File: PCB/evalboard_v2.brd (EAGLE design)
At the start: 85.7 x 65.5 mm, 63 parts, among them IC1 BQ24074, IC2 LTC3113EFE#PBF, IC3 LTC3130IUDC-1#PBF#2, J1 2604-1102, J2 PJ-031D, J3 2604-1102, Q1 DMP3056L-7#2, Q2 DMG3402L-7, Q3 DMP3056L-7#2, Q4 DMG3402L-7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

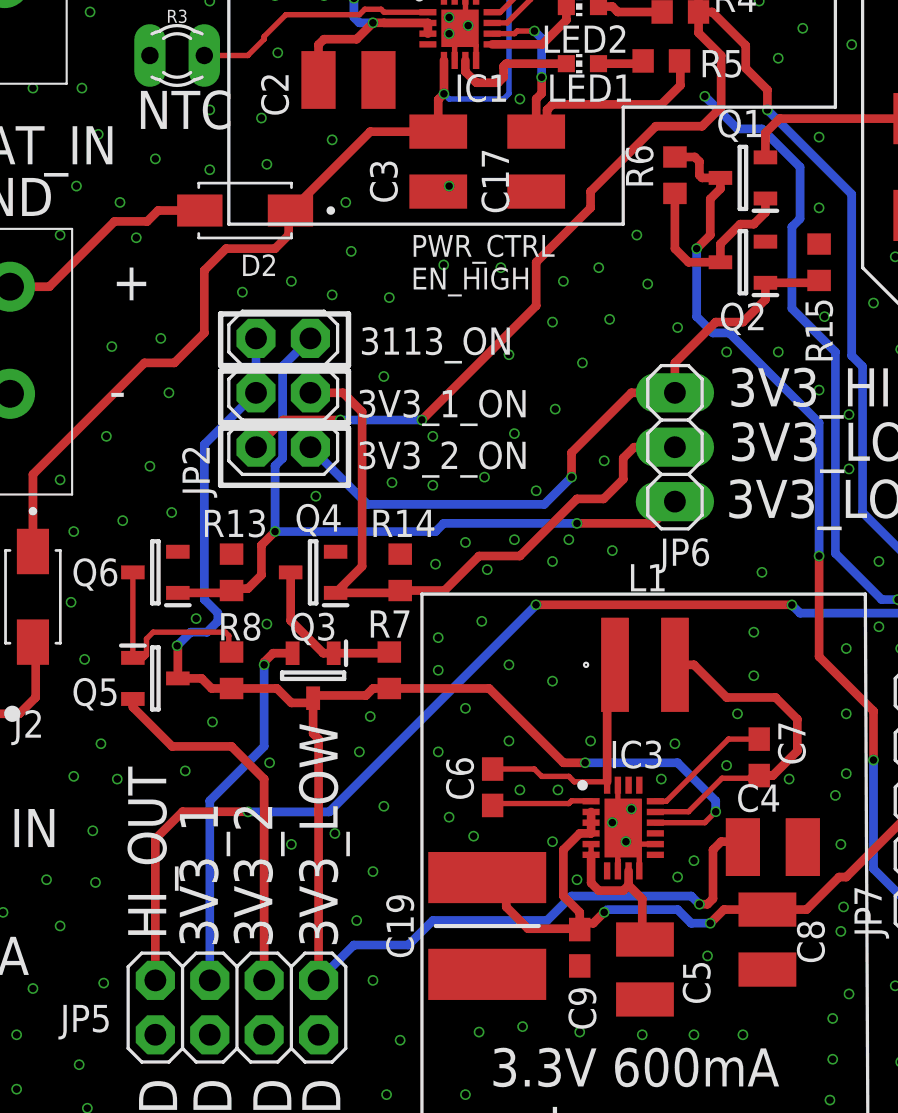
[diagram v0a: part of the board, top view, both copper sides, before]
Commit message: Fixed MOSFETs, VS1, VS2, updated README
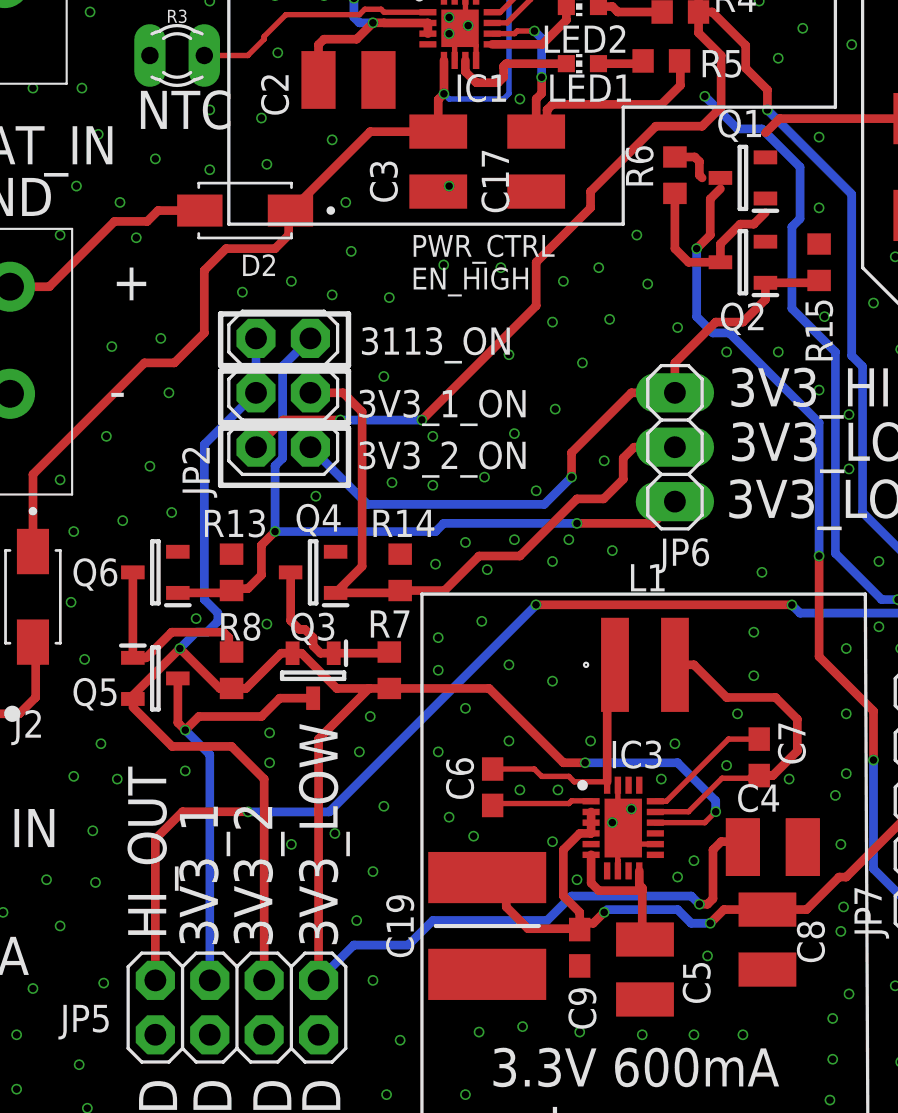
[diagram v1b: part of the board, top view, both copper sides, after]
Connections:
- removed net VCC: C5.2, IC3.5, IC3.6, IC3.9
- new net VCC_3130: C5.2, IC3.10, IC3.5, IC3.6
- net 3113_IN: now also Q1.3; no longer Q1.2
- net 3V3_LOW: now also Q3.2, Q5.2; no longer Q3.3, Q5.3
- net 3V3_LOW_1: no longer Q5.2
- net 3V3_LOW_2: now also Q3.3, Q5.3; no longer Q3.2
- net BQ_OUT3: now also Q1.2; no longer Q1.3
- net GND: now also IC3.9; no longer IC3.10
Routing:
- net VCC: track 7.34 -> 0.00 mm
- net VCC_3130: track 0.00 -> 7.17 mm
- net 3V3_LOW: track 87.5 -> 91.7 mm
- net 3V3_LOW_2: track 17.4 -> 21.3 mm
- net GND: track 27.3 -> 25.7 mm, vias 379 -> 378
- net BQ_OUT3: track 42.6 -> 41.2 mm
- net 3113_IN: track 80.0 -> 78.9 mm
- net N$10: track 9.19 -> 8.53 mm
